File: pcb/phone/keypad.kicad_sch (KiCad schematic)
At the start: 29 parts, among them SW1 SKQGABE010, SW10 SKQGABE010, SW11 SKQGABE010, SW12 SKQGABE010, SW13 SKQGABE010, SW14 SKQGABE010, SW15 SKQGABE010, SW16 SKQGABE010, SW17 SKQGABE010, SW18 SKQGABE010, SW19 SKQGABE010, SW2 SKQGABE010, SW20 SKQGABE010, SW3 SKQGABE010, SW4 SKQGABE010, SW5 SKQGABE010, SW6 SKQGABE010, SW7 SKQGABE010, SW8 SKQGABE010, SW9 SKQGABE010

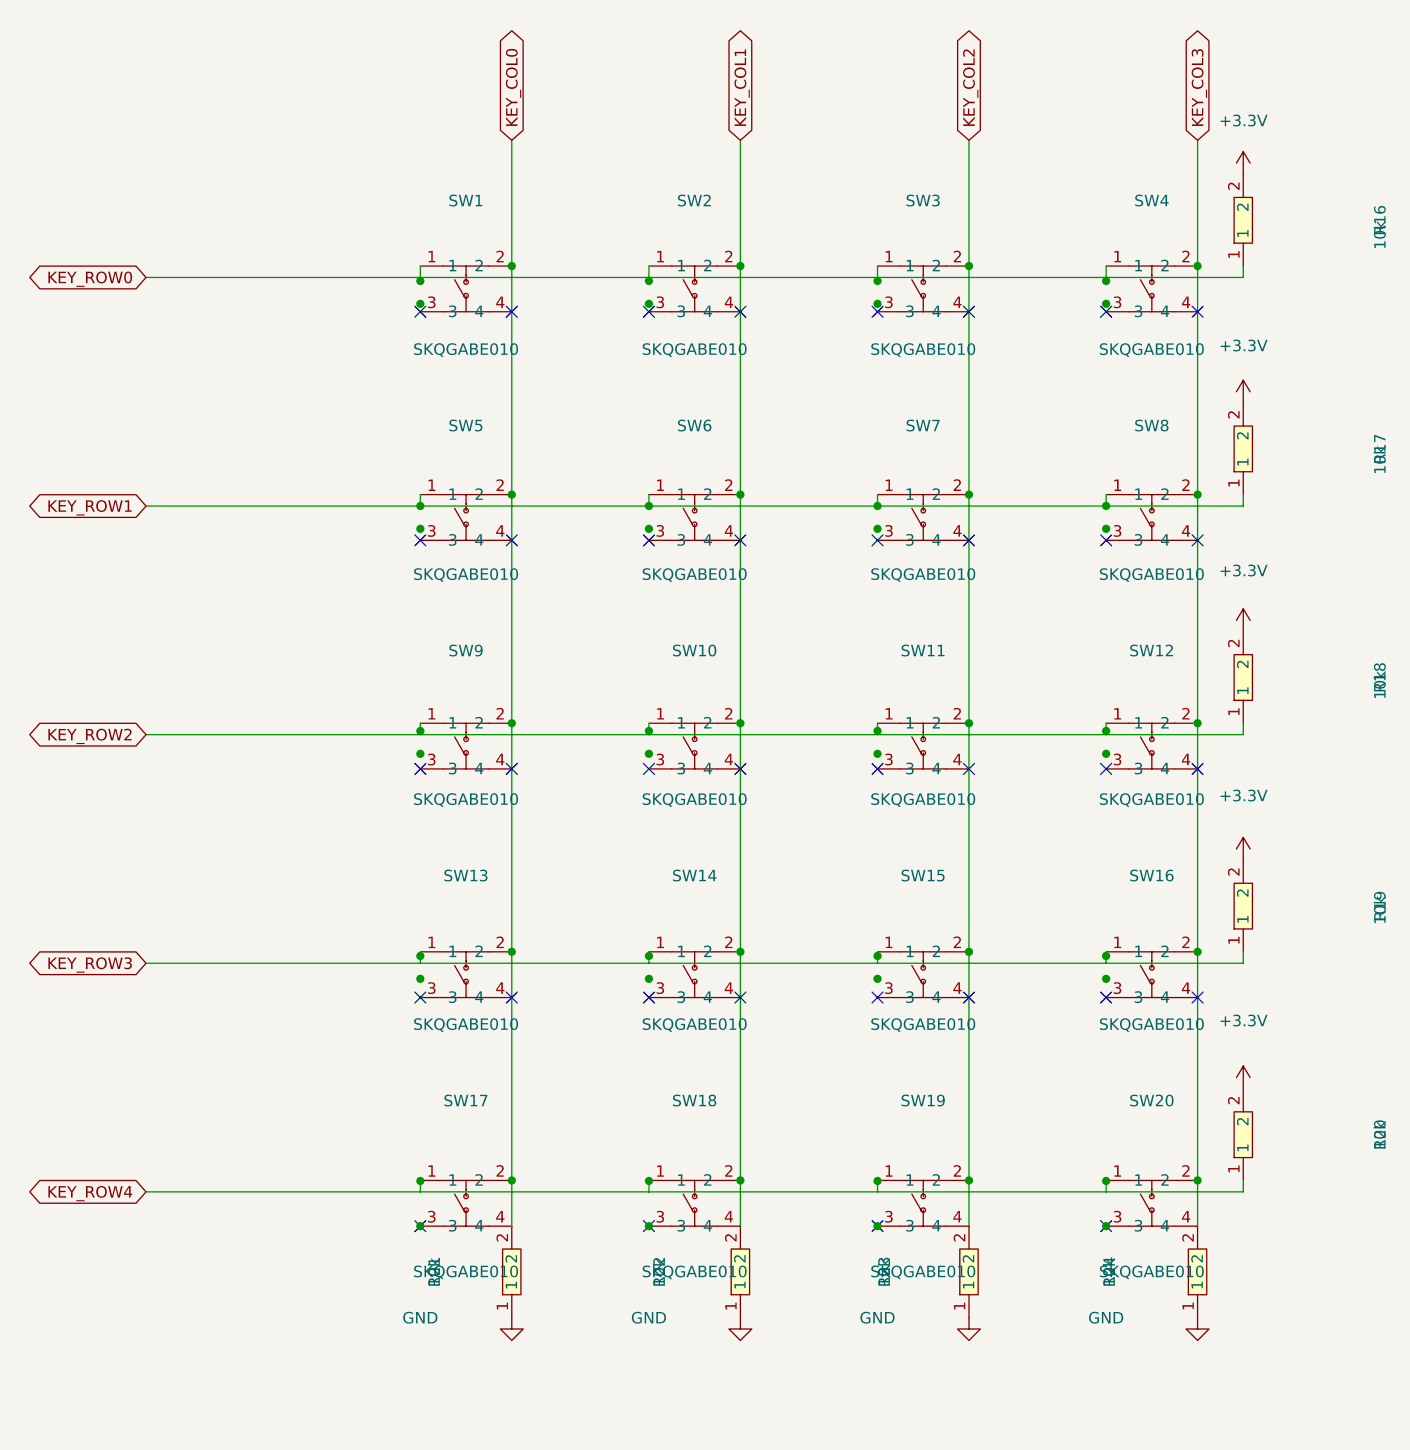
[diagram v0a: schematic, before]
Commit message: User edits: keypad rewiring, sheet reorder, ERC severity reverts, R24 fix
Keypad (keypad.kicad_sch):
- Rotated all 20 switches 270 degrees for vertical contact orientation
- Wired all 4 pins on each switch (pins 1&2 to column, pins 3&4 to row)
- Removed all 37 no_connect markers on pins 3&4
- Cleaned up to 25.4mm (1-inch) grid spacing
- Added pull-down resistors to all 4 columns (was only KEY_COL3)

Root sheet (phone.kicad_sch):
- Reordered sub-sheet blocks (Display_Daughter before SIM_SD)
- Cleaned up PWR_FLAG symbol formatting/indentation
- Reordered PWR_FLAG and +BATT symbol placement

MCU sheet (mcu.kicad_sch):
- Repositioned +3.3V power symbol (#PWR32) at pin 190.5,200.66

Project settings (phone.kicad_pro):
- Reverted ERC suppressions: endpoint_off_grid, isolated_pin_label,
  lib_symbol_mismatch back to warning (want actual fixes, not ignores)
- Added SW2-20 to used designators
- Reordered sheets list (Display_Daughter before SIM_SD)

Other sheets (codec, display, display_daughter, sim_sd):
- KiCad editor reformatting upon save

Generated with [Devin](https://devin.ai)

Co-Authored-By: Devin <158243242+devin-ai-integration[bot]@users.noreply.github.com>
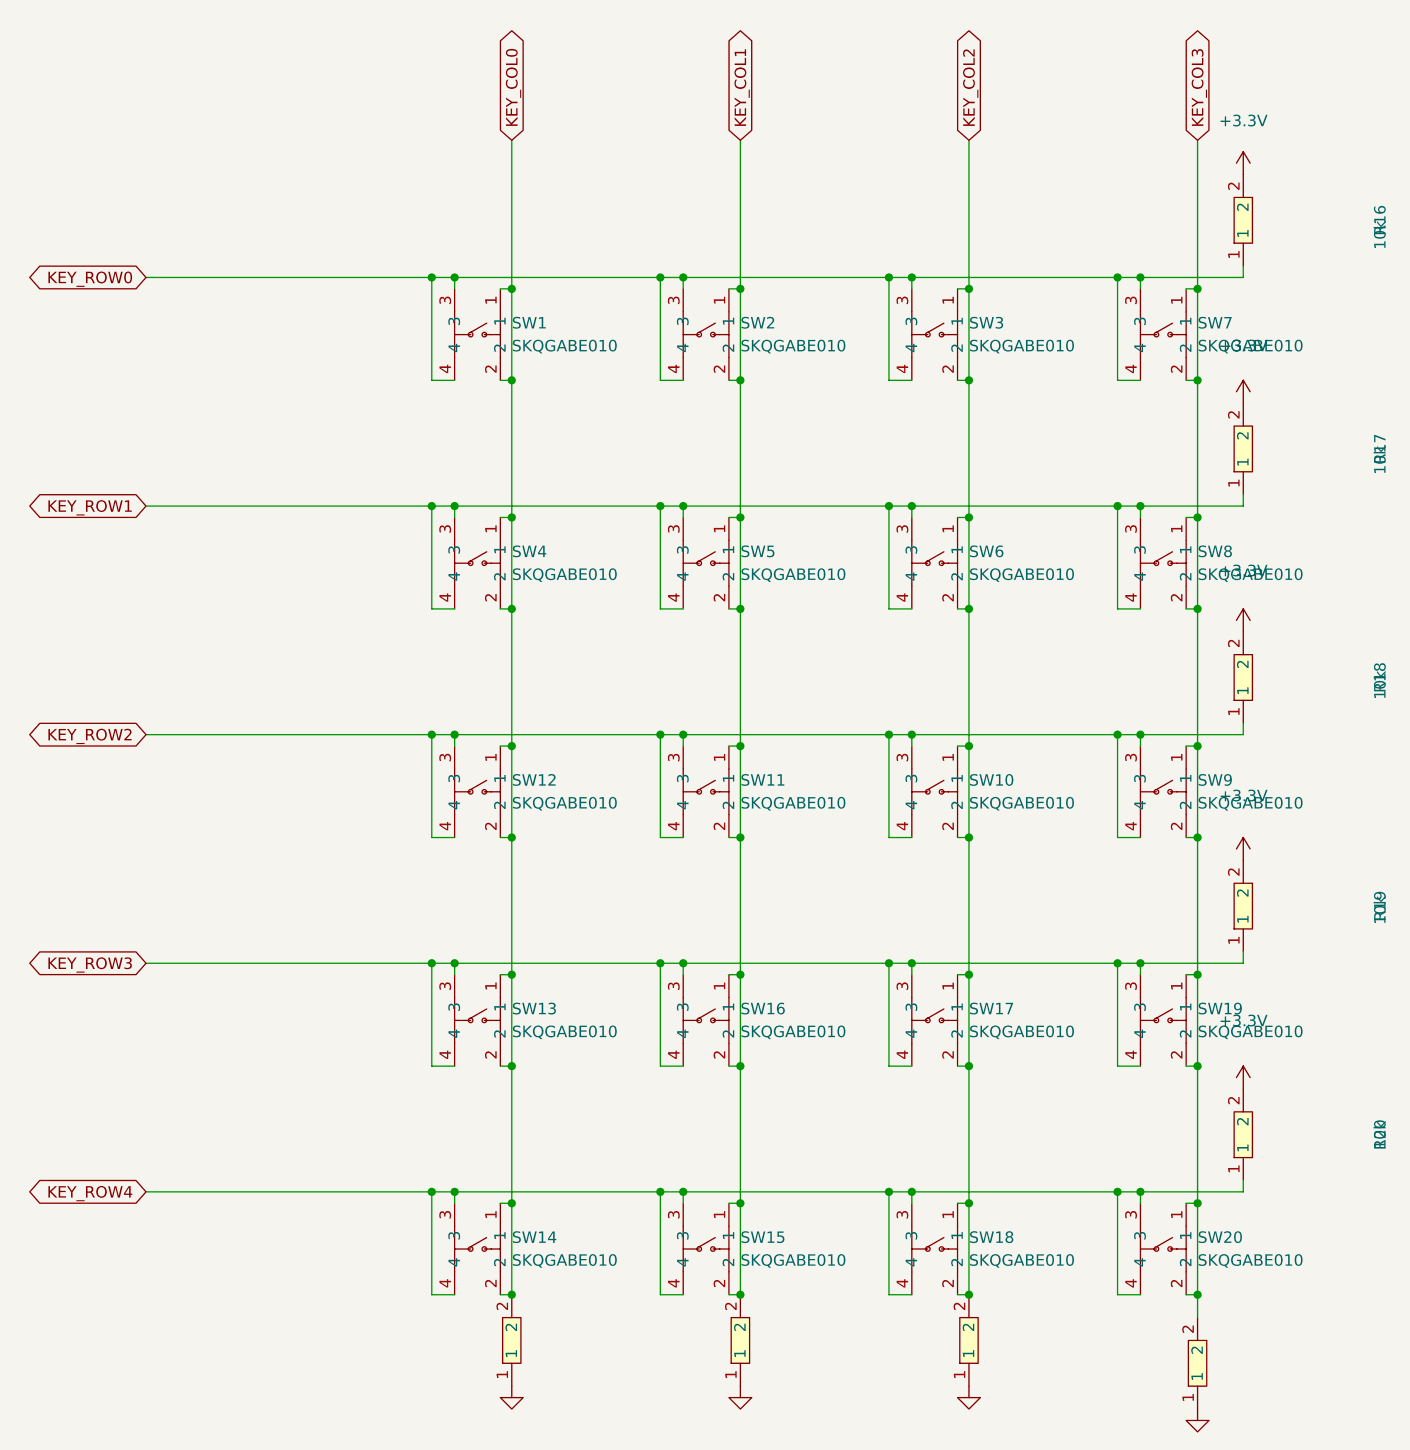
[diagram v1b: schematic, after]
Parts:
- removed R21, R22, R23: 10k, symbol passives:RC0603JR-0710KL
- added R25, R26, R27: 10k, symbol passives:RC0603JR-0710KL
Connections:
- net GND: now also R25.1, R26.1, R27.1
- net KEY_COL0: now also SW1.1, SW12.1, SW12.2, SW13.1, SW14.1, SW14.2, SW4.1, SW4.2, R27.2; no longer SW17.2, SW17.4, SW5.2, SW9.2
- net KEY_COL1: now also SW11.1, SW11.2, SW15.1, SW15.2, SW16.1, SW16.2, SW2.1, SW5.1, SW5.2, R26.2; no longer SW10.2, SW14.2, SW18.2, SW18.4, SW6.2
- net KEY_COL2: now also SW10.1, SW10.2, SW17.1, SW17.2, SW18.1, SW18.2, SW3.1, SW6.1, SW6.2, R25.2; no longer SW11.2, SW15.2, SW19.2, SW19.4, SW7.2
- net KEY_COL3: now also SW19.1, SW19.2, SW20.1, SW7.1, SW7.2, SW8.1, SW9.1, SW9.2; no longer SW12.2, SW16.2, SW20.4, SW4.2
- net KEY_ROW0: now also SW1.3, SW1.4, SW2.3, SW2.4, SW3.3, SW3.4, SW7.3, SW7.4; no longer SW1.1, SW2.1, SW3.1, SW4.1
- net KEY_ROW1: now also SW4.3, SW4.4, SW5.3, SW5.4, SW6.3, SW6.4, SW8.3, SW8.4; no longer SW5.1, SW6.1, SW7.1, SW8.1
- net KEY_ROW2: now also SW10.3, SW10.4, SW11.3, SW11.4, SW12.3, SW12.4, SW9.3, SW9.4; no longer SW10.1, SW11.1, SW12.1, SW9.1
- net KEY_ROW3: now also SW13.3, SW13.4, SW16.3, SW16.4, SW17.3, SW17.4, SW19.3, SW19.4; no longer SW13.1, SW14.1, SW15.1, SW16.1
- net KEY_ROW4: now also SW14.3, SW14.4, SW15.3, SW15.4, SW18.3, SW18.4, SW20.3, SW20.4; no longer SW17.1, SW18.1, SW19.1, SW20.1
- no-connect marks 36 -> 0
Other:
- moved on the sheet: SW1
